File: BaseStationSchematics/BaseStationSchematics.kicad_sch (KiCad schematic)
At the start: 5 parts, among them J1 Conn_01x02_Pin, J2 Conn_01x02_Pin, J3 Conn_01x01_Socket, U1 DOIT-ESP32-DEVKIT-V1, U2 Ra01_Breakout_Module-Ra01_Bre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

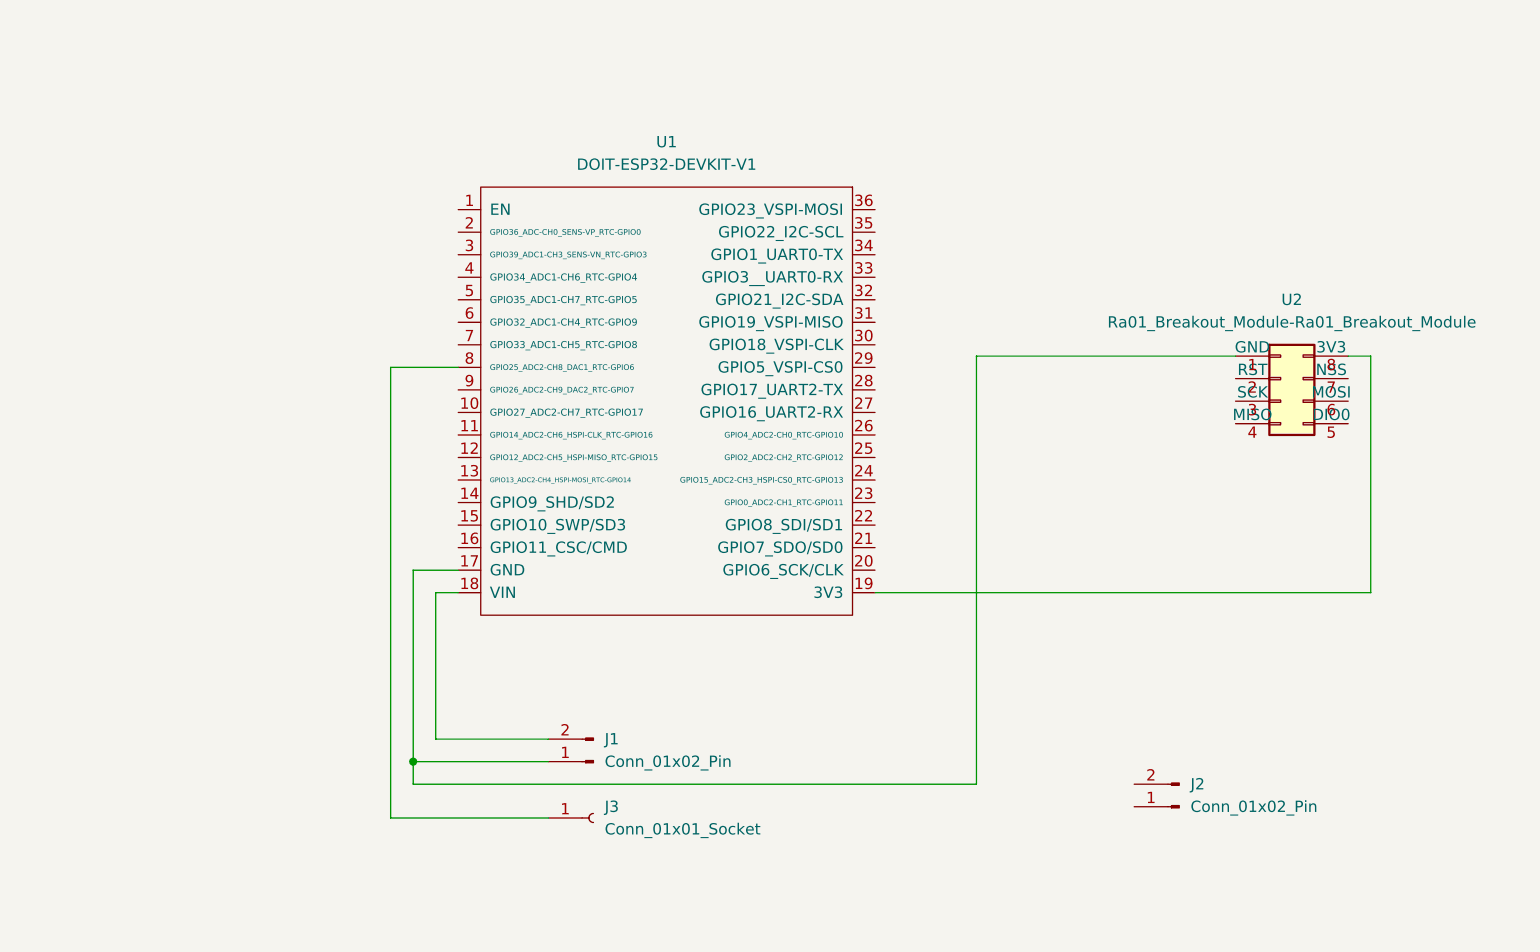
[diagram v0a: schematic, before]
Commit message: Schematic mostly created, added LoRa watchdog task
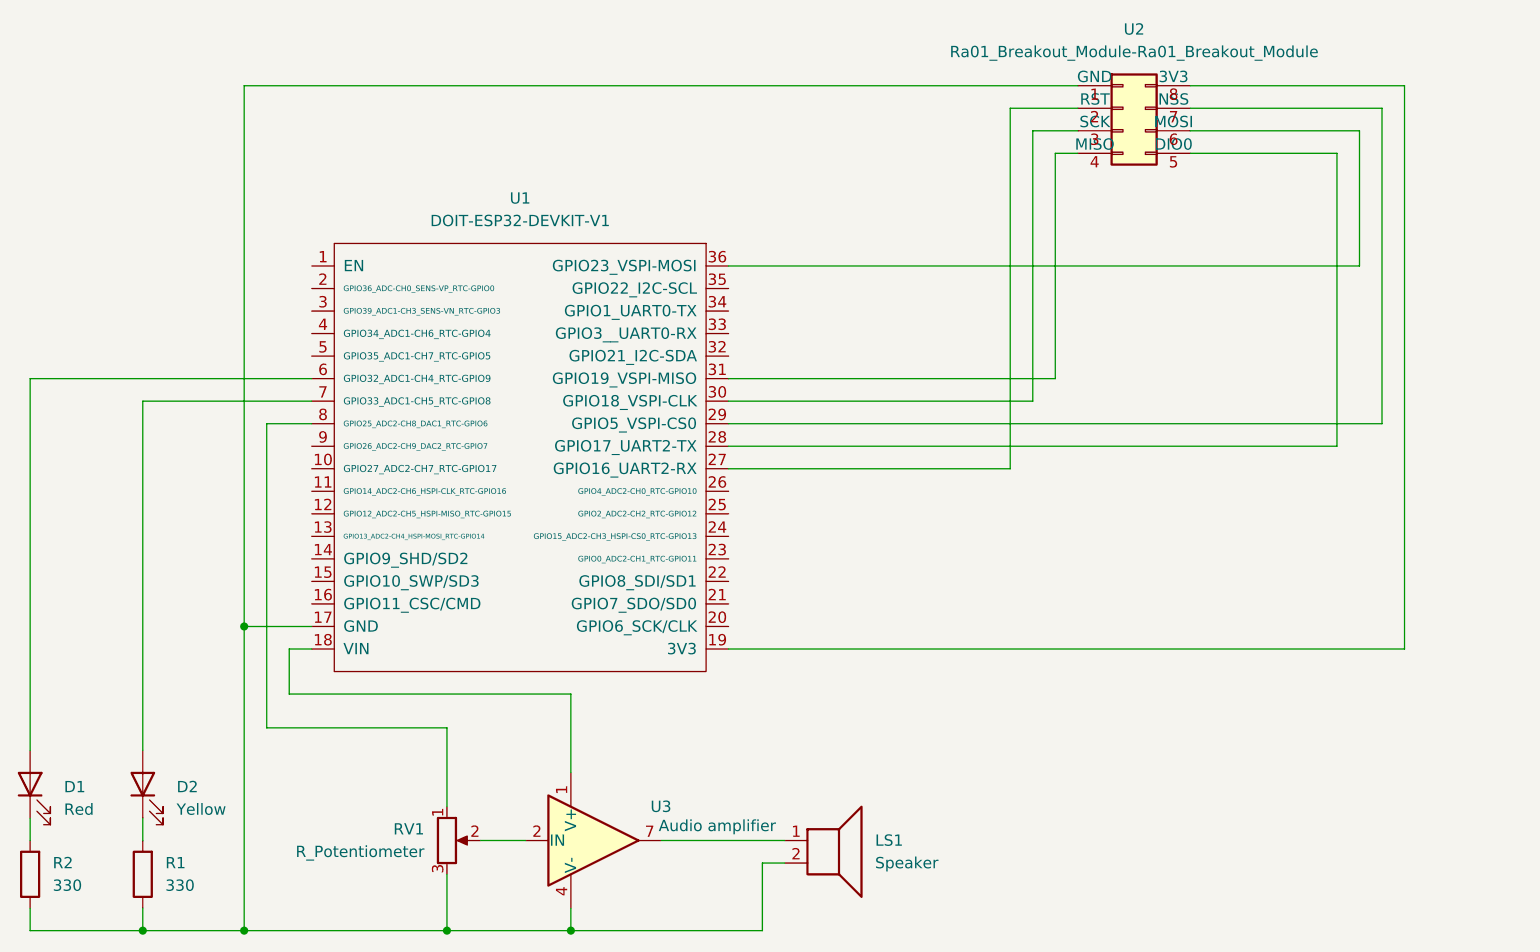
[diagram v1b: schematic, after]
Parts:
- removed J1, J2: Conn_01x02_Pin, symbol Connector:Conn_01x02_Pin
- removed J3: Conn_01x01_Socket, symbol Connector:Conn_01x01_Socket
- added D1: Red, symbol Device:LED
- added D2: Yellow, symbol Device:LED
- added LS1: Speaker, symbol Device:Speaker
- added R1, R2: 330, symbol Device:R
- added RV1: R_Potentiometer, symbol Device:R_Potentiometer
- added U3: Audio amplifier, Package_DIP:DIP-8_W7.62mm, symbol Amplifier_Buffer:EL2001CN
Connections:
- net at U1.8 (GPIO25_ADC2-CH8_DAC1_RTC-GPIO6): now also RV1.1
- net at U1.17 (GND), U2.1 (GND): now also LS1.2, R1.1, R2.1, RV1.3, U3.4 (V-)
- net at U1.18 (VIN): now also U3.1 (V+)
- net at U2.2 (RST): now also U1.27 (GPIO16_UART2-RX)
- net at U2.3 (SCK): now also U1.30 (GPIO18_VSPI-CLK)
- net at U2.4 (MISO): now also U1.31 (GPIO19_VSPI-MISO)
- net at U2.5 (DIO0): now also U1.28 (GPIO17_UART2-TX)
- net at U2.6 (MOSI): now also U1.36 (GPIO23_VSPI-MOSI)
- net at U2.7 (NSS): now also U1.29 (GPIO5_VSPI-CS0)
- net at U1.6 (GPIO32_ADC1-CH4_RTC-GPIO9): now also D1.2 (A)
- net at U1.7 (GPIO33_ADC1-CH5_RTC-GPIO8): now also D2.2 (A)
- new net: D1.1 (K), R2.2
- new net: D2.1 (K), R1.2
- new net: LS1.1, U3.7
- new net: RV1.2, U3.2 (IN)
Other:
- company: (none) -> Jotham Gates
- title: (none) -> Farm Base Station Schematic
- moved on the sheet: U1, U2

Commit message: Added github pages doxygen action
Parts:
- D1: value Red -> White
- D2: value Yellow -> Red
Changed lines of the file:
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@@
       (effects (font (size 1.27 1.27)) (justify right))
     )
-    (property "Value" "Red" (at 81.28 126.0475 90)
+    (property "Value" "White" (at 81.28 126.0475 90)
       (effects (font (size 1.27 1.27)) (justify right))
     )
@@
       (effects (font (size 1.27 1.27)) (justify right))
     )
-    (property "Value" "Yellow" (at 93.98 126.0475 90)
+    (property "Value" "Red" (at 93.98 126.0475 90)
       (effects (font (size 1.27 1.27)) (justify right))
     )

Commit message: Added images and improved readme
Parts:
- R1, R2: value 330 -> 82
- RV1: value R_Potentiometer -> 20k
- U3: value Audio amplifier -> LM386N based audio amplifier
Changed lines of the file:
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@@
       (effects (font (size 1.27 1.27)) (justify right))
     )
-    (property "Value" "330" (at 92.71 134.62 0)
+    (property "Value" "82" (at 92.71 134.62 0)
       (effects (font (size 1.27 1.27)) (justify right))
     )
@@
   (symbol (lib_id "Amplifier_Buffer:EL2001CN") (at 140.97 129.54 0) (unit 1)
     (in_bom yes) (on_board yes) (dnp no)
-    (property "Reference" "U3" (at 148.59 125.73 0)
-      (effects (font (size 1.27 1.27)))
-    )
-    (property "Value" "Audio amplifier" (at 154.94 127.8891 0)
+    (property "Reference" "U3" (at 142.24 120.65 0)
+      (effects (font (size 1.27 1.27)))
+    )
+    (property "Value" "LM386N based audio amplifier" (at 156.21 123.19 0)
       (effects (font (size 1.27 1.27)))
     )
@@
       (effects (font (size 1.27 1.27)) (justify right))
     )
-    (property "Value" "R_Potentiometer" (at 121.92 130.81 0)
+    (property "Value" "20k" (at 121.92 130.81 0)
       (effects (font (size 1.27 1.27)) (justify right))
     )
@@
       (effects (font (size 1.27 1.27)) (justify right))
     )
-    (property "Value" "330" (at 80.01 134.62 0)
-      (effects (font (size 1.27 1.27)) (justify right))
-    )
+    (property "Value" "82" (at 80.01 134.62 0)
+      (effects (font (size 1.27 1.27)) (justify right))
+    )
